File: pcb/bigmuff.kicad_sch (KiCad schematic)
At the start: 46 parts, among them Q1 BC549, Q2 BC549, Q3 BC549, Q5 BC549

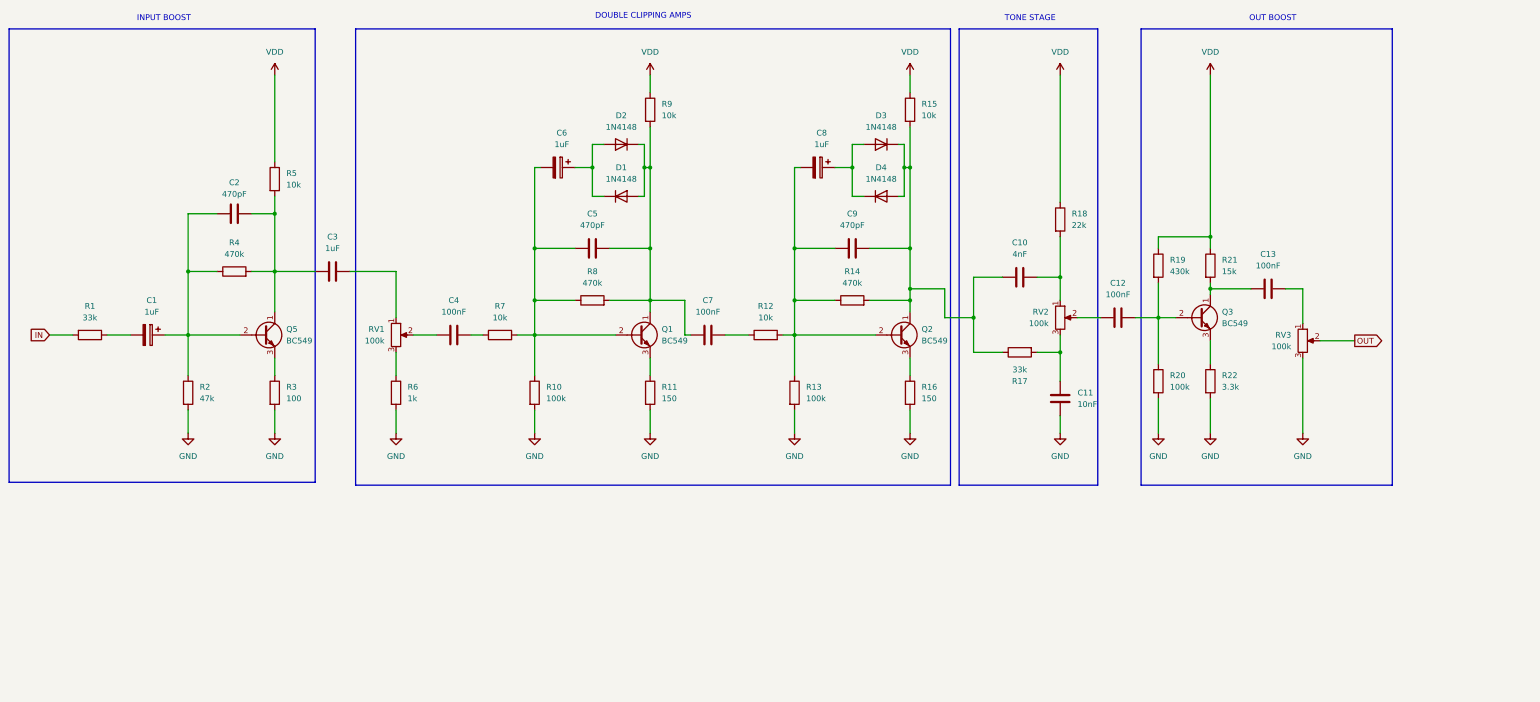
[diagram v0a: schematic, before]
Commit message: Update Schematic, add resistor footprints
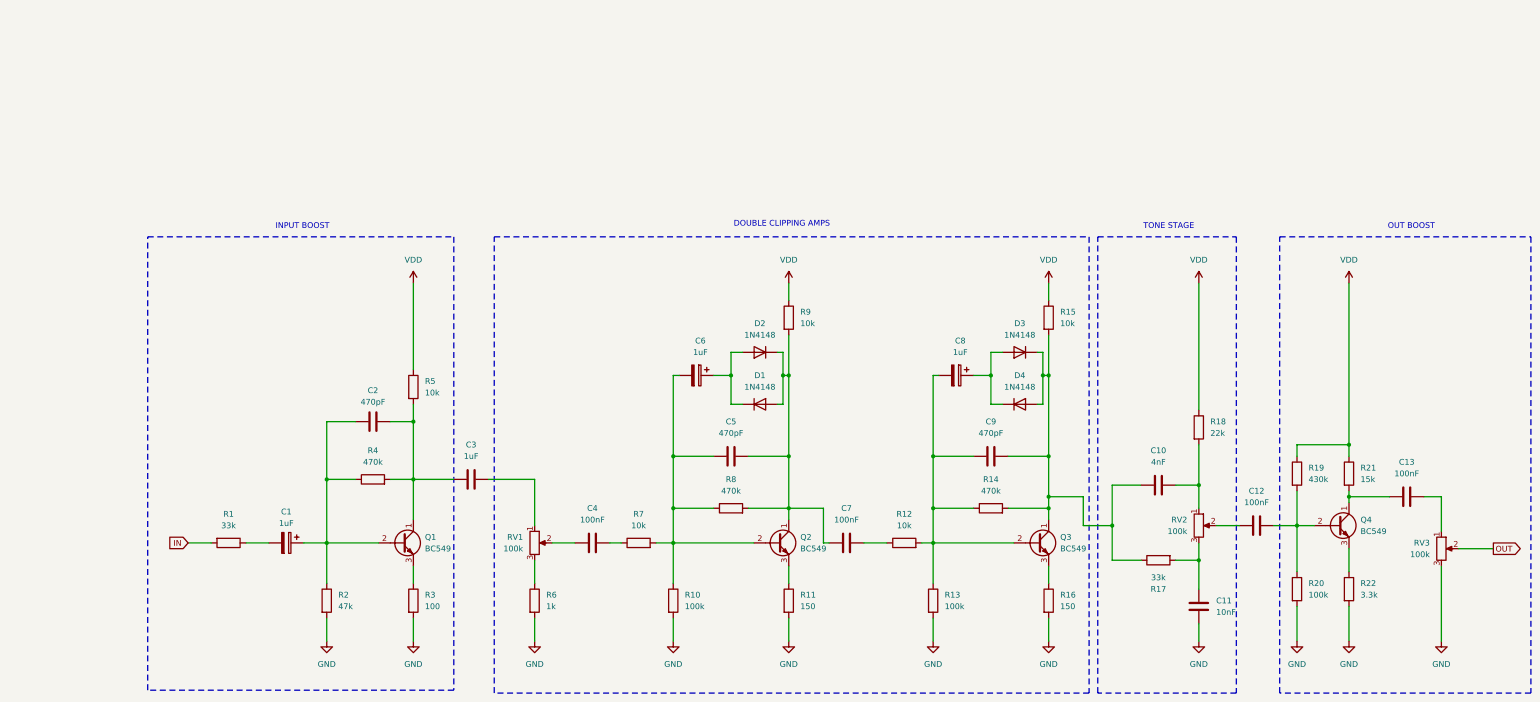
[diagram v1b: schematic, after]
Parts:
- Q1: renamed from Q5; footprint Package_TO_SOT_THT:TO-92_Inline -> Package_TO_SOT_THT:TO-92_Inline_Wide
- Q2: renamed from Q1; footprint Package_TO_SOT_THT:TO-92_Inline -> Package_TO_SOT_THT:TO-92_Inline_Wide
- Q3: renamed from Q2; footprint Package_TO_SOT_THT:TO-92_Inline -> Package_TO_SOT_THT:TO-92_Inline_Wide
- Q4: renamed from Q3; footprint Package_TO_SOT_THT:TO-92_Inline -> Package_TO_SOT_THT:TO-92_Inline_Wide
- R1, R10, R11, R12, R13, R14, R15, R16, R17, R18, R19, R2, R20, R21, R22, R3, R4, R5, R6, R7, R8, R9, RV1, RV2, RV3: footprint (none) -> Resistor_THT:R_Axial_DIN0207_L6.3mm_D2.5mm_P7.62mm_Horizontal
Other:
- company: (none) -> UF AES
- title: (none) -> Big Muff Pi
- moved on the sheet: C1, C10, C11, C12, C13, C2, C3, C4, C5, C6, C7, C8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
